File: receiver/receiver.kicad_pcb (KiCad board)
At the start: 4 copper layers, 26.2 x 28 mm, 24 parts, among them J1 CONN_04SCREW, J2 Conn_02x05_Counter_Clockwise, SW1 SW_DIP_x03, U1 10118194-MICRO-USB, U2 LM3671MF-3.3/NOPBMF05A-M, U3 SN74LVC1T45DBVRDBV6-M, U4 SN74LVC1T45DBVRDBV6-M

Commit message: Updated BOM
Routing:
- net GND: track 31.2 -> 34.9 mm, vias 40 -> 39
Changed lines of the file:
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@@
-	)
-	(segment
-		(start 99.4625 135)
-		(end 99.4625 136.7625)
-		(width 0.75)
-		(layer "F.Cu")
-		(net 2)
 	)
 	(segment
@@
 	)
 	(segment
+		(start 99.4625 136.7625)
+		(end 100 137.3)
+		(width 1)
+		(layer "F.Cu")
+		(net 2)
+	)
+	(segment
 		(start 107 132.5)
 		(end 107 132.422998)
@@
 		(end 121.4 119.6)
 		(width 0.3048)
-		(layer "F.Cu")
-		(net 2)
-	)
-	(segment
-		(start 99.4625 136.7625)
-		(end 100 137.3)
-		(width 0.75)
 		(layer "F.Cu")
 		(net 2)
@@
 		(net 2)
 	)
+	(segment
+		(start 99.4625 135)
+		(end 99.4625 136.7625)
+		(width 1)
+		(layer "F.Cu")
+		(net 2)
+	)
 	(via
 		(at 113.6425 123.29)
@@
 	)
 	(via
-		(at 122.2 134.2)
-		(size 0.6)
-		(drill 0.3)
-		(layers "F.Cu" "B.Cu")
-		(net 2)
-	)
-	(via
 		(at 97.8 131.4)
 		(size 0.6)
@@
 	)
 	(via
-		(at 122.25 116.45)
-		(size 0.6)
-		(drill 0.3)
-		(layers "F.Cu" "B.Cu")
-		(net 2)
-	)
-	(via
 		(at 116.5 125.195)
 		(size 0.5532)
@@
 	)
 	(via
+		(at 121.775 134.825)
+		(size 0.6)
+		(drill 0.3)
+		(layers "F.Cu" "B.Cu")
+		(net 2)
+	)
+	(via
 		(at 119 123.9)
 		(size 0.6)
@@
 	)
 	(segment
-		(start 122.25 134.15)
-		(end 122.2 134.2)
-		(width 0.3048)
+		(start 122.2 117.4)
+		(end 120.2 117.4)
+		(width 0.6)
 		(layer "B.Cu")
 		(net 2)
@@
 	(segment
 		(start 103.7945 129.965)
-		(end 103.2 129.3705)
-		(width 0.3048)
+		(end 104.74 129.965)
+		(width 0.6)
 		(layer "B.Cu")
 		(net 2)
@@
 	(segment
 		(start 122.25 115.75)
-		(end 122.25 116.45)
-		(width 0.3048)
+		(end 122.25 117.35)
+		(width 0.6)
+		(layer "B.Cu")
+		(net 2)
+	)
+	(segment
+		(start 122.25 134.35)
+		(end 121.775 134.825)
+		(width 0.6)
+		(layer "B.Cu")
+		(net 2)
+	)
+	(segment
+		(start 122.25 117.35)
+		(end 122.2 117.4)
+		(width 0.6)
+		(layer "B.Cu")
+		(net 2)
+	)
+	(segment
+		(start 103.2 129.3705)
+		(end 103.7945 129.965)
+		(width 0.6)
 		(layer "B.Cu")
 		(net 2)
@@
 	(segment
 		(start 122.25 132.75)
-		(end 122.25 134.15)
-		(width 0.3048)
-		(layer "B.Cu")
-		(net 2)
-	)
-	(segment
-		(start 104.74 129.965)
-		(end 103.7945 129.965)
-		(width 0.3048)
+		(end 122.25 134.35)
+		(width 0.6)
 		(layer "B.Cu")
 		(net 2)
@@
 	)
 	(segment
+		(start 120.98 132.75)
+		(end 120.98 134.18)
+		(width 0.6)
+		(layer "B.Cu")
+		(net 3)
+	)
+	(segment
 		(start 120.98 134.18)
 		(end 121 134.2)
-		(width 0.3048)
-		(layer "B.Cu")
-		(net 3)
-	)
-	(segment
-		(start 120.98 132.75)
-		(end 120.98 134.18)
-		(width 0.3048)
-		(layer "B.Cu")
-		(net 3)
+		(width 0.6)
+		(layer "B.Cu")
+		(net 3)

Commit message: Saving previous version of receiver
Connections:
- U$2 pad 10: unconnected-(U$2-IO25-Pad10) -> Net-(LED1-A)
- U$2 pad 26: BRIGHTNESS -> unconnected-(U$2-IO4-Pad26)
- U$2 pad 6: Net-(LED1-A) -> unconnected-(U$2-IO34-Pad6)
- U$2 pad 7: unconnected-(U$2-IO35-Pad7) -> BRIGHTNESS
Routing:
- net BRIGHTNESS: track 15.4 -> 21.0 mm
- net Net-(LED1-A): track 18.9 -> 17.5 mm
- net unconnected-(U$2-IO4-Pad26): track 0.00 -> 0.86 mm
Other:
- board text added: "RVL Receiver v1.2 © Bryan Hughes August 2025"
- board text removed: "RVL Receiver v1.0 © Bryan Hughes January 2025"

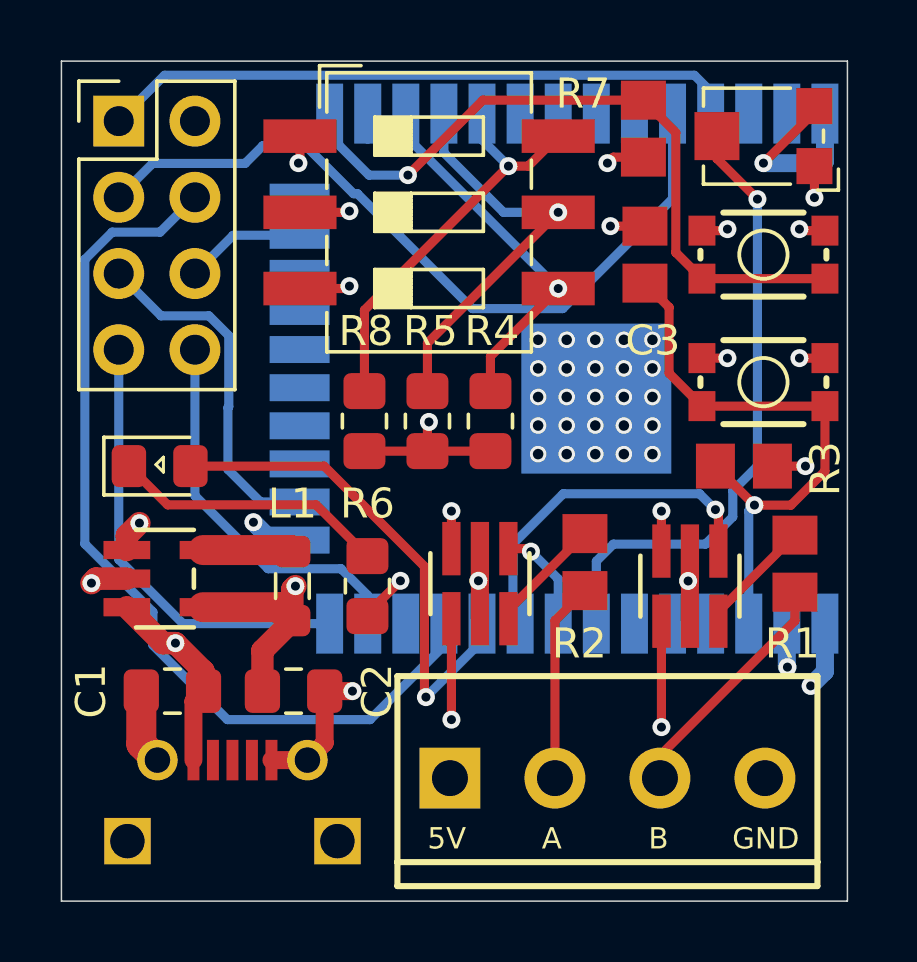
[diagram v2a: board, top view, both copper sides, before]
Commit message: Finished first draft of new receiver
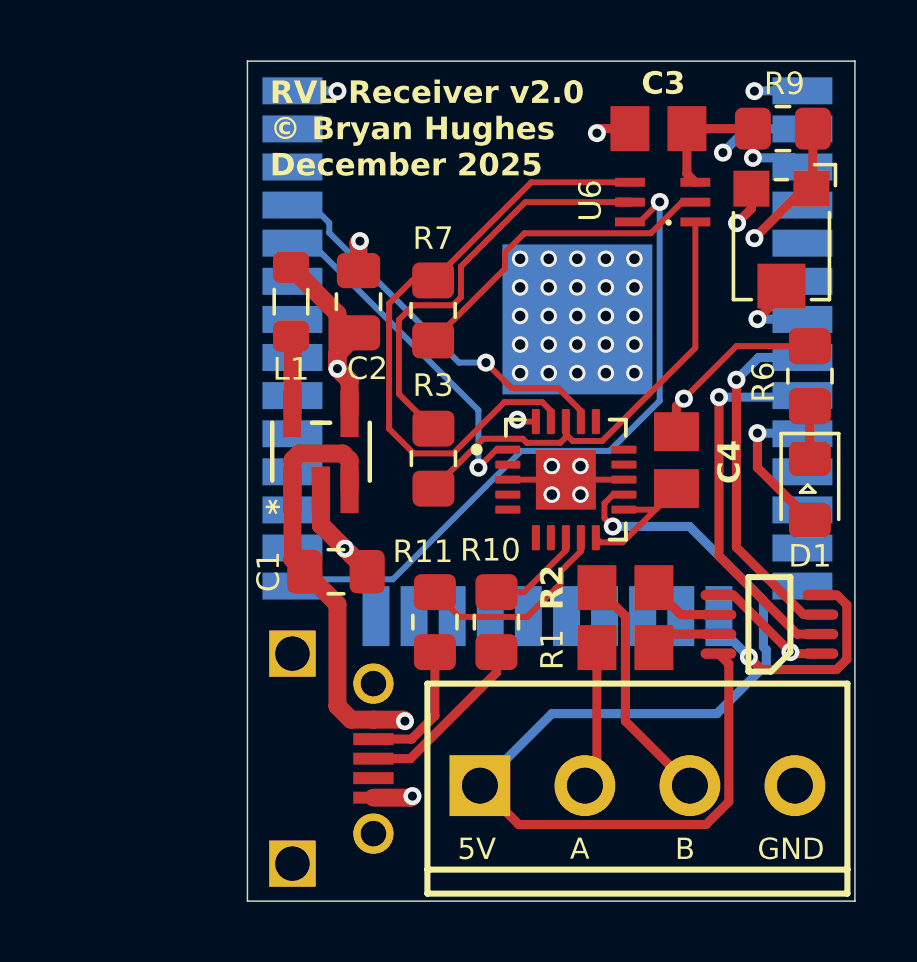
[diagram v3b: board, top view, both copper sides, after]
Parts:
- removed J2: Conn_02x05_Counter_Clockwise, Connector_PinHeader_2.54mm:PinHeader_2x04_P2.54mm_Vertical
- removed LED1: Power, LED_SMD:LED_0805_2012Metric_Pad1.15x1.40mm_HandSolder
- removed R4, R5, R8: 10k, Resistor_SMD:R_0805_2012Metric_Pad1.20x1.40mm_HandSolder
- removed S2, S3: MOMENTARY-SWITCH-SPST-2-SMD-4.6X2.8MM, receiver:TACTILE_SWITCH_SMD_4.6X2.8MM
- removed SW1: SW_DIP_x03, Button_Switch_SMD:SW_DIP_SPSTx03_Slide_6.7x9.18mm_W8.61mm_P2.54mm_LowProfile
- removed U4: SN74LVC1T45DBVRDBV6-M, receiver:DBV6-M
- added C4: 1uF, receiver:C0805, F.Cu at (117.3, 127.3)
- added D1: LED, LED_SMD:LED_0805_2012Metric_Pad1.15x1.40mm_HandSolder, F.Cu at (121.8, 128.3)
- added R10: 27, Resistor_SMD:R_0805_2012Metric_Pad1.20x1.40mm_HandSolder, F.Cu at (111.3, 132.7)
- added R11: 27, Resistor_SMD:R_0805_2012Metric_Pad1.20x1.40mm_HandSolder, F.Cu at (109.2, 132.7)
- added R9: 10k, Resistor_SMD:R_0805_2012Metric_Pad1.20x1.40mm_HandSolder, F.Cu at (120.8, 116.2)
- added U5: FT231XQ-R, receiver:QFN50P400X400X80-21N, F.Cu at (113.6, 128.0)
- added U6: MBT3904DW1T1G, receiver:SOT236, F.Cu at (116.8, 118.7)
- R3, R7: footprint receiver:R0805 -> Resistor_SMD:R_0805_2012Metric_Pad1.20x1.40mm_HandSolder
- U3: value SN74LVC1T45DBVRDBV6-M -> SN74LVC2T45DCTRE4; footprint receiver:DBV6-M -> receiver:DCT0008A_L
- moved R6 16.3 mm to (121.8, 124.5), turned to -90 degrees
- moved C2 13.2 mm to (106.7, 122.0), turned to 90 degrees
- moved U$2 13.1 mm to (113.0, 115.0), turned to 180 degrees
- moved R3 10.4 mm to (109.2, 127.2), turned to 90 degrees
- moved L1 9.48 mm to (104.5, 122.0), turned to 90 degrees
- moved R7 9.27 mm to (109.2, 122.3)
- moved C1 6.75 mm to (106.0, 131.0), turned to 0 degrees
- moved U2 6.71 mm to (105.5, 127.0), turned to 90 degrees
- moved R1 6.31 mm to (115.6, 133.6), turned to 0 degrees
- moved C3 4.22 mm to (116.7, 116.2), turned to 180 degrees
- moved RV1 3.62 mm to (120.8, 120.0), turned to -90 degrees
- moved U1 3.40 mm to (104.5, 137.2), turned to -90 degrees
- moved U3 2.94 mm to (120.4, 132.8), turned to 180 degrees
- moved R2 1.60 mm to (115.6, 131.6), turned to 0 degrees
- moved J1 1.03 mm to (110.8, 138.2)
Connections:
- C3 pad 1: Net-(U$2-EN) -> EN
- R1 pad 1: Net-(U3-A) -> Net-(J1-Pad2)
- R1 pad 2: Net-(J1-Pad3) -> Net-(U3-B1)
- R2 pad 1: Net-(U4-A) -> Net-(J1-Pad3)
- R2 pad 2: Net-(J1-Pad2) -> Net-(U3-B2)
- R3 pad 1: Net-(U$2-EN) -> Net-(U5-DTR#)
- R3 pad 2: +3.3V -> Net-(R3-Pad2)
- R7 pad 1: Net-(U$2-IO0) -> Net-(U5-RTS#)
- R7 pad 2: +3.3V -> Net-(R7-Pad2)
- U$2 pad 11: GPIO26 -> unconnected-(U$2-IO26-Pad11)
- U$2 pad 13: TMS -> unconnected-(U$2-IO14-Pad13)
- U$2 pad 14: TDI -> unconnected-(U$2-IO12-Pad14)
- U$2 pad 16: TCK -> unconnected-(U$2-IO13-Pad16)
- U$2 pad 23: TDO -> unconnected-(U$2-IO15-Pad23)
- U$2 pad 25: Net-(U$2-IO0) -> IO0
- U$2 pad 27: DIP3 -> unconnected-(U$2-IO16-Pad27)
- U$2 pad 28: DIP2 -> unconnected-(U$2-IO17-Pad28)
- U$2 pad 29: DIP1 -> unconnected-(U$2-IO5-Pad29)
- U$2 pad 3: Net-(U$2-EN) -> EN
- U1 pad 2: unconnected-(U1-D--Pad2) -> USB_D-
- U1 pad 3: unconnected-(U1-D+-Pad3) -> USB_D+
- U3 pad 1: +5V -> +3.3V
- U3 pad 2: GND -> LED_DATA
- U3 pad 3: Net-(U3-A) -> LED_CLOCK
- U3 pad 4: LED_DATA -> GND
- U3 pad 5: GND -> +3.3V
- U3 pad 6: +3.3V -> Net-(U3-B2)
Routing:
- net +5V: track 14.5 -> 53.0 mm, vias 4 -> 2
- net GPIO26: track 30.8 -> 0.00 mm
- net Net-(U$2-IO0): track 23.6 -> 0.00 mm, vias 1 -> 0
- net IO0: track 0.00 -> 22.7 mm, vias 0 -> 1
- net Net-(U5-RTS#): track 0.00 -> 20.8 mm
- net Net-(U$2-EN): track 19.8 -> 0.00 mm, vias 1 -> 0
- net BRIGHTNESS: track 21.0 -> 2.94 mm
- net Net-(U5-DTR#): track 0.00 -> 16.3 mm
- net TDI: track 14.9 -> 0.00 mm
- net Net-(R3-Pad2): track 0.00 -> 14.4 mm
- net RXD: track 25.8 -> 11.6 mm, vias 0 -> 1
- net DIP2: track 13.7 -> 0.00 mm, vias 1 -> 0
- net DIP1: track 13.7 -> 0.00 mm, vias 1 -> 0
- net TMS: track 12.9 -> 0.00 mm
- net Net-(D1-A): track 17.5 -> 5.13 mm
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- removed copper zone on In2.Cu, net +5V
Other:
- board size 26.2 x 28 mm -> 20.2 x 28 mm
- board text added: "RVL Receiver v2.0 © Bryan Hughes December 2025"
- board text removed: "RVL Receiver v1.2 © Bryan Hughes August 2025"
